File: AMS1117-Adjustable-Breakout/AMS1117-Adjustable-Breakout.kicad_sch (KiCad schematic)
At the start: 13 parts, among them J1 Input, J2 Output, U1 AMS1117

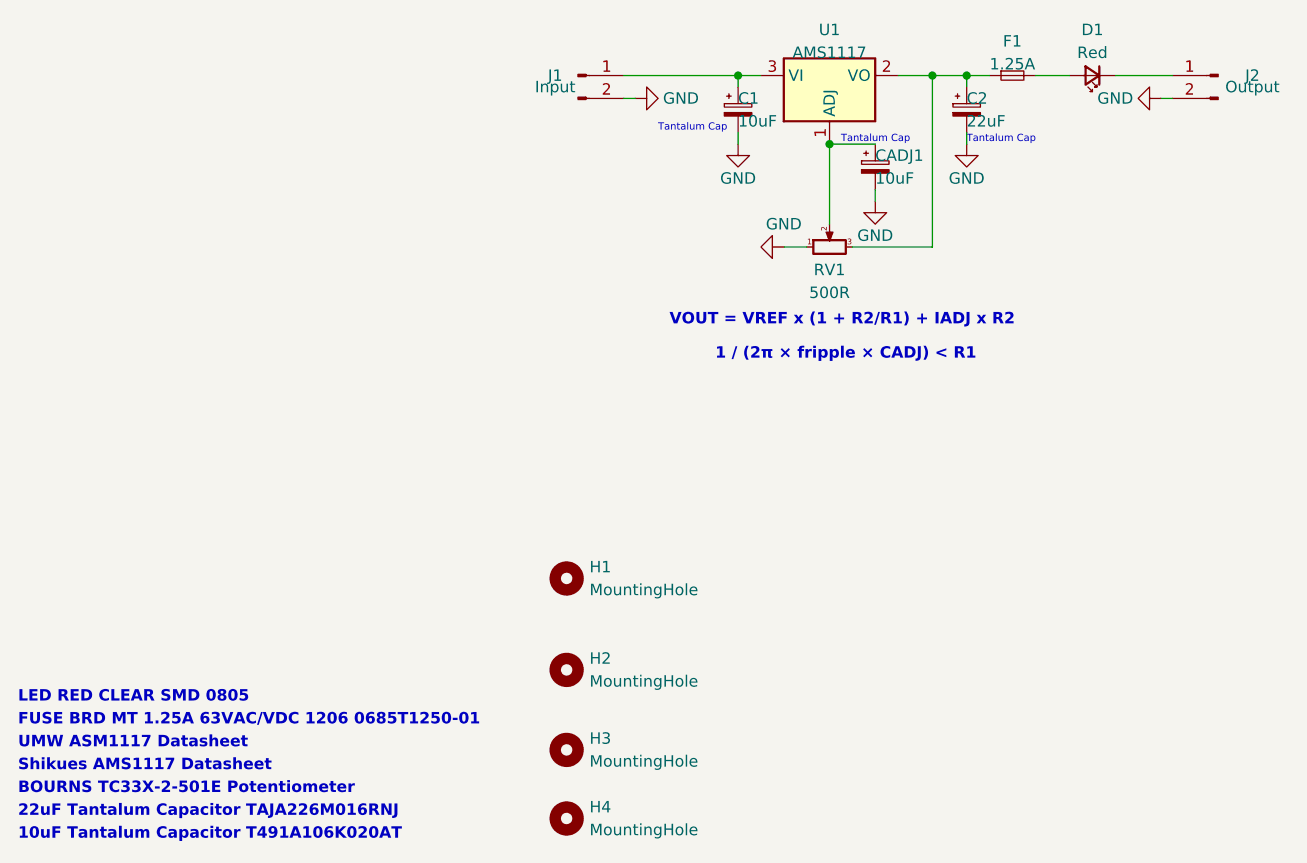
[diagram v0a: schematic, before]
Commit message: REG1117 Update
AD 23/08/23:
Datasheet for REG1117 Regulator added.
1000R Trimmer option added to schematic.
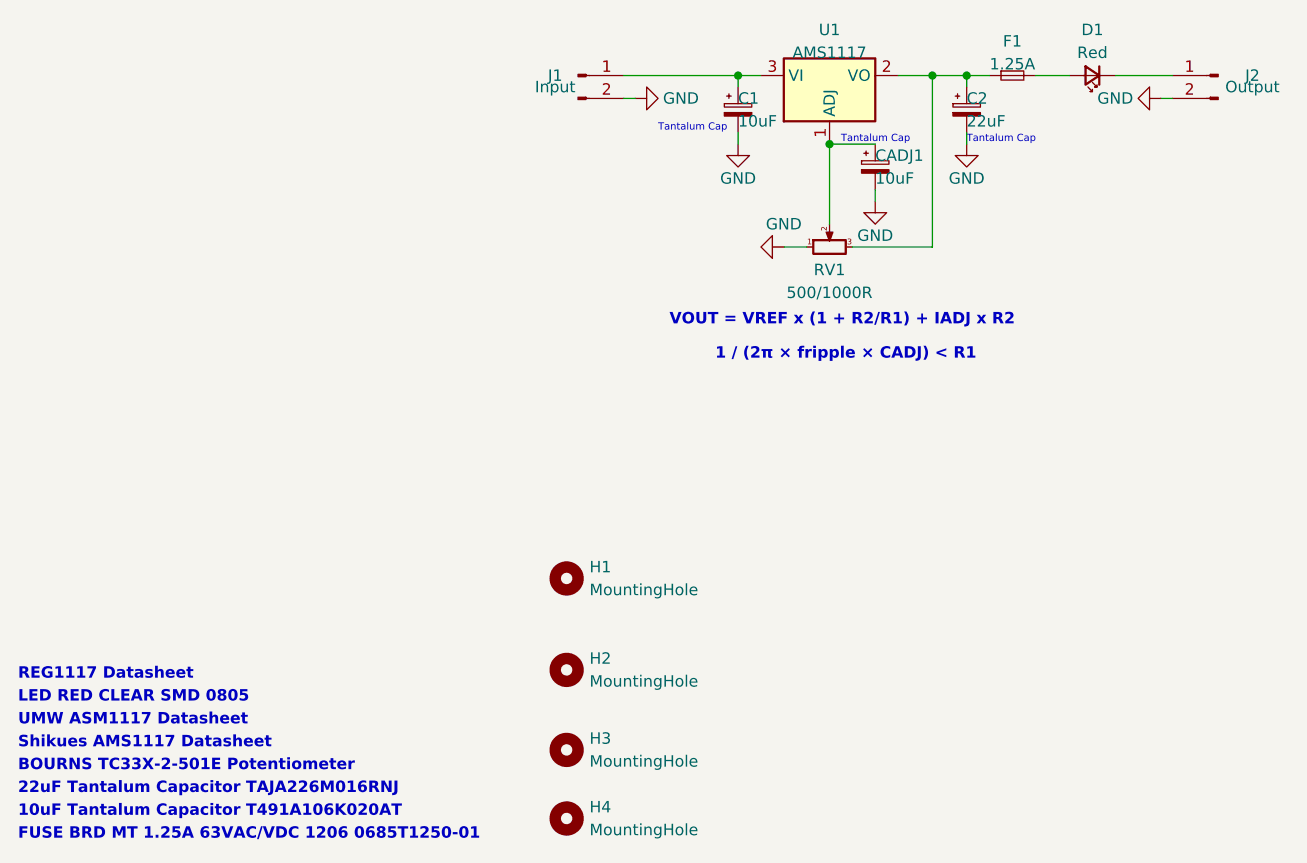
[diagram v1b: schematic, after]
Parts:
- RV1: value 500R -> 500/1000R
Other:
- note added: "REG1117 Datasheet"
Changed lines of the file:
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@@
     )
+  )
+  (text "REG1117 Datasheet" (at 12.7 118.11 0)
+    (effects (font (size 1.27 1.27) (thickness 0.254) bold) (justify left bottom) (href "https://rocelec.widen.net/view/pdf/f0nffzgjqp/sbvs001d.pdf?t.download=true&u=5oefqw"))
   )
   (text "Tantalum Cap" (at 104.14 58.42 0)
@@
     (effects (font (size 0.8 0.8)) (justify left bottom))
   )
-  (text "10uF Tantalum Capacitor T491A106K020AT" (at 12.7 135.89 0)
+  (text "10uF Tantalum Capacitor T491A106K020AT" (at 12.7 133.35 0)
     (effects (font (size 1.27 1.27) (thickness 0.254) bold) (justify left bottom) (href "https://connect.kemet.com:7667/gateway/IntelliData-ComponentDocumentation/1.0/download/datasheet/T491A106K020AT"))
   )
-  (text "UMW ASM1117 Datasheet" (at 12.7 125.73 0)
+  (text "UMW ASM1117 Datasheet" (at 12.7 123.19 0)
     (effects (font (size 1.27 1.27) (thickness 0.254) bold) (justify left bottom) (href "https://media.digikey.com/pdf/Data%20Sheets/UTD%20Semi%20PDFs/AMS1117.pdf"))
   )
@@
     (effects (font (size 1.27 1.27) bold (color 255 87 82 1)) (justify left bottom))
   )
-  (text "FUSE BRD MT 1.25A 63VAC/VDC 1206 0685T1250-01" (at 12.7 123.19 0)
+  (text "FUSE BRD MT 1.25A 63VAC/VDC 1206 0685T1250-01" (at 12.7 135.89 0)
     (effects (font (size 1.27 1.27) (thickness 0.254) bold) (justify left bottom) (href "https://www.belfuse.com/resources/datasheets/circuitprotection/ds-cp-c1t-series.pdf"))
   )
-  (text "Shikues AMS1117 Datasheet" (at 12.7 128.27 0)
+  (text "Shikues AMS1117 Datasheet" (at 12.7 125.73 0)
     (effects (font (size 1.27 1.27) bold) (justify left bottom) (href "https://datasheet.lcsc.com/szlcsc/2001081204_Shikues-AMS1117-1-2_C475600.pdf"))
   )
-  (text "22uF Tantalum Capacitor TAJA226M016RNJ" (at 12.7 133.35 0)
+  (text "22uF Tantalum Capacitor TAJA226M016RNJ" (at 12.7 130.81 0)
     (effects (font (size 1.27 1.27) (thickness 0.254) bold) (justify left bottom) (href "https://datasheets.kyocera-avx.com/TAJ.pdf"))
   )
@@
     (effects (font (size 1.27 1.27) bold (color 255 87 82 1)) (justify left bottom))
   )
-  (text "BOURNS TC33X-2-501E Potentiometer" (at 12.7 130.81 0)
+  (text "BOURNS TC33X-2-501E Potentiometer" (at 12.7 128.27 0)
     (effects (font (size 1.27 1.27) bold) (justify left bottom) (href "https://datasheet.lcsc.com/lcsc/2208261830_BOURNS-TC33X-2-501E_C720649.pdf"))
   )
@@
       (effects (font (size 1.27 1.27)))
     )
-    (property "Value" "500R" (at 102.87 74.93 90)
-      (effects (font (size 1.27 1.27)))
-    )
+    (property "Value" "500/1000R" (at 102.87 74.93 90)
+      (effects (font (size 1.27 1.27)))
+    )
